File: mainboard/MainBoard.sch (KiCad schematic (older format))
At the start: 38 parts, among them J1 CONN_1x4, J2 CONN_2X3, J3 CONN_2X3, J5 SWDEBUG_CONNECTOR, J7 CONN_2X12, U1 VX07805-1000, U2 TPS2115A, U3 ld1117s33

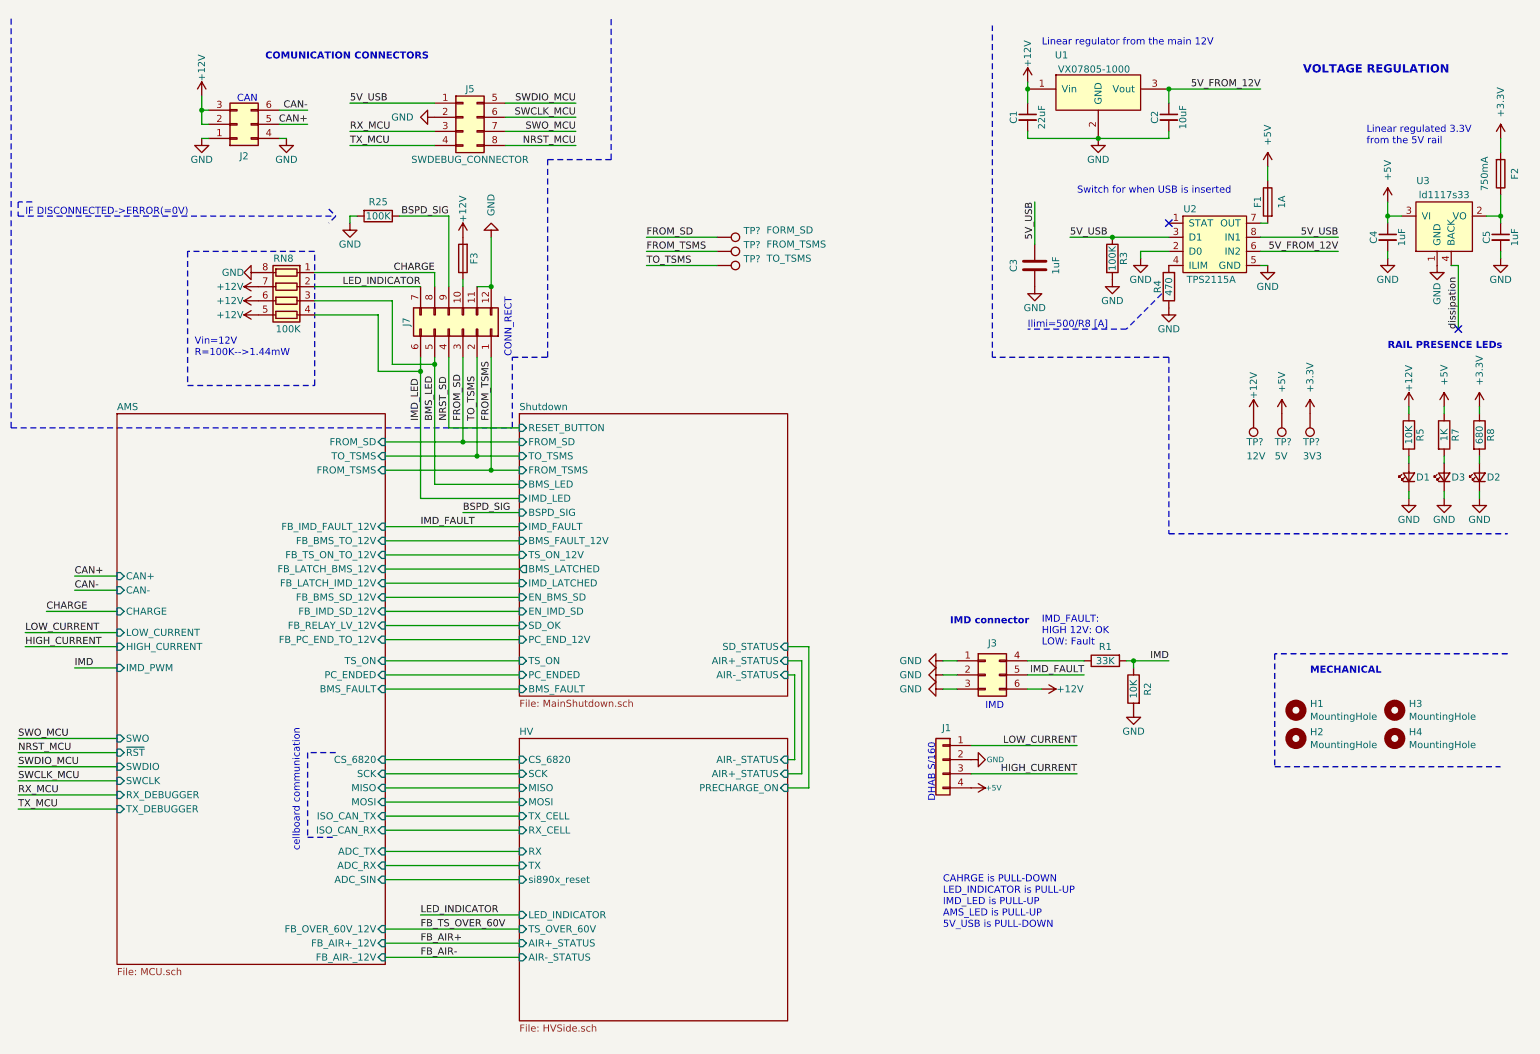
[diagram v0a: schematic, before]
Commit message: adding testpoints
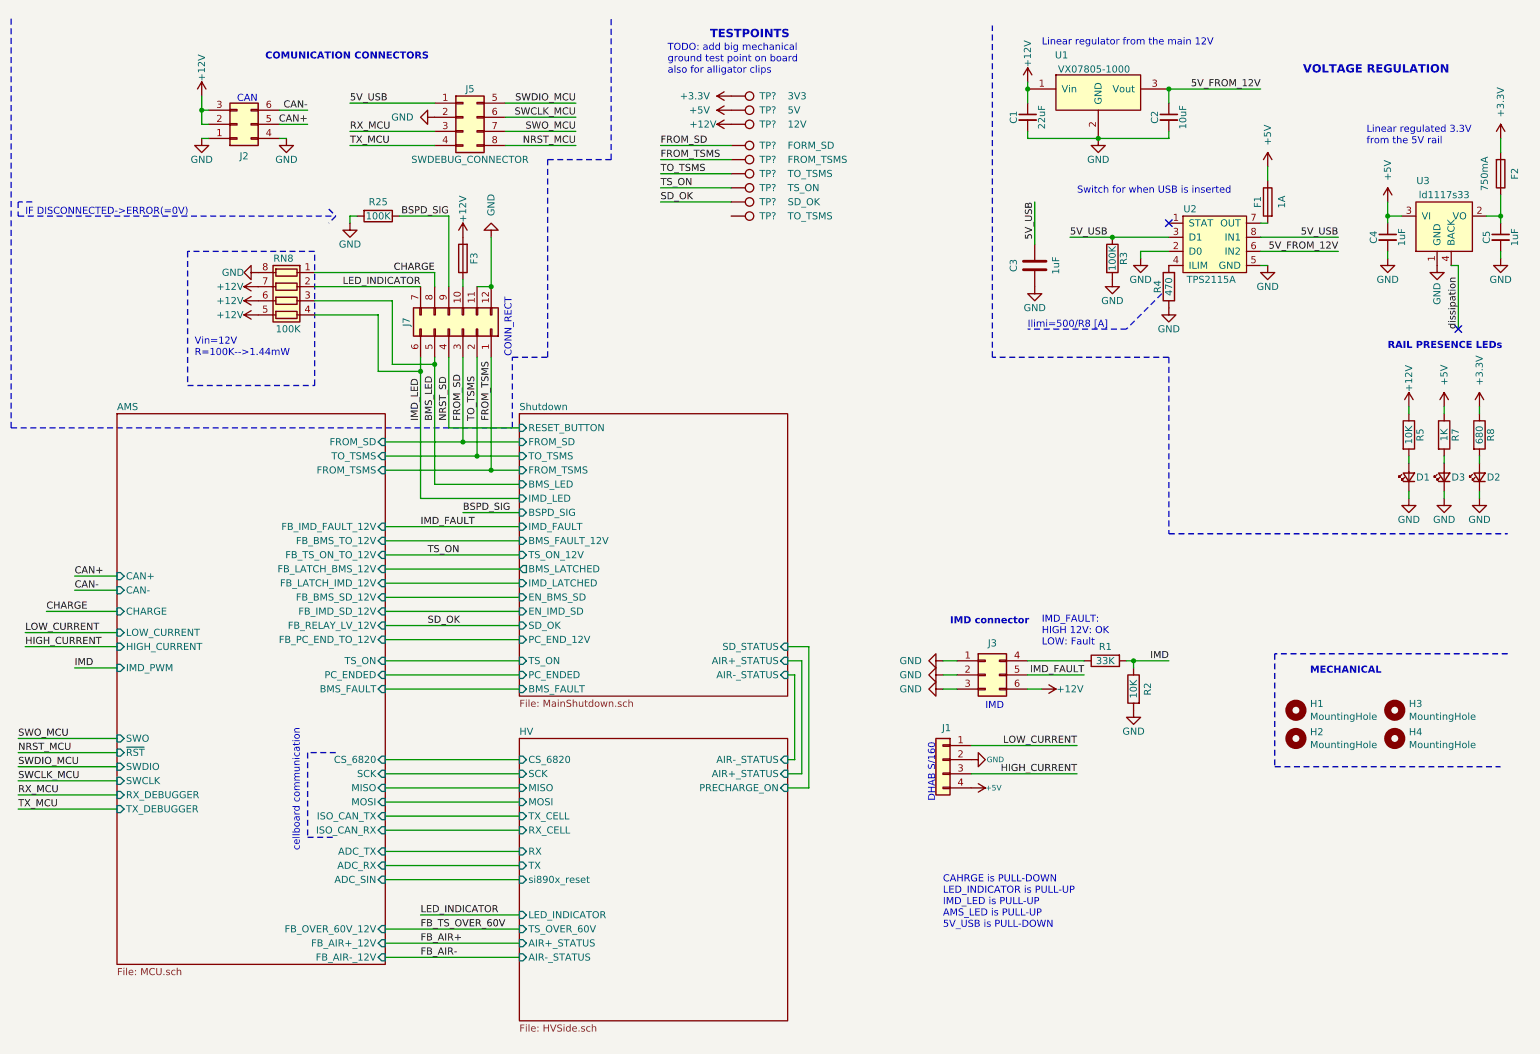
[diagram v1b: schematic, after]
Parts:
- removed TP?: 3V3, symbol Connector:TestPoint
- removed TP?: 5V, symbol Connector:TestPoint
- removed TP?: 12V, symbol Connector:TestPoint
- added TP?: TS_ON, symbol Connector:TestPoint
- added TP?: SD_OK, symbol Connector:TestPoint
- added TP?: TO_TSMS, symbol Connector:TestPoint
- added TP?: 3V3, symbol Connector:TestPoint
- added TP?: 5V, symbol Connector:TestPoint
- added TP?: 12V, symbol Connector:TestPoint
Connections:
- net +12V: now also TP?.1
- net +3V3: now also TP?.1
- net +5V: now also TP?.1
- new net SD_OK: TP?.1
- new net TS_ON: TP?.1
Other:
- note added: "TESTPOINTS"
- note added: "TODO: add big mechanical \nground test point on board\nalso for alligator clips"
- moved on the sheet: TP?
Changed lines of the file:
@@
 Text Notes 7800 5000 0    50   ~ 0
 IMD_FAULT:\nHIGH 12V: OK\nLOW: Fault
-Text Label 5000 2100 0    50   ~ 0
+Text Label 5100 1450 0    50   ~ 0
 FROM_SD
-Text Label 5000 2200 0    50   ~ 0
+Text Label 5100 1550 0    50   ~ 0
 FROM_TSMS
-Text Label 5000 2300 0    50   ~ 0
+Text Label 5100 1650 0    50   ~ 0
 TO_TSMS
 $Comp
 L Connector:TestPoint TP?
 U 1 1 605C7740
-P 5500 2100
-F 0 "TP?" V 5454 2288 50  0000 L CNN
-F 1 "FORM_SD" V 5450 2450 50  0000 L CNN
-F 2 "" H 5700 2100 50  0001 C CNN
-F 3 "~" H 5700 2100 50  0001 C CNN
-	1    5500 2100
+P 5600 1450
+F 0 "TP?" V 5600 1650 50  0000 L CNN
+F 1 "FORM_SD" V 5600 1850 50  0000 L CNN
+F 2 "" H 5800 1450 50  0001 C CNN
+F 3 "~" H 5800 1450 50  0001 C CNN
+	1    5600 1450
 	0    1    1    0
 $EndComp
@@
 L Connector:TestPoint TP?
 U 1 1 605C7DFE
-P 5500 2200
-F 0 "TP?" V 5454 2388 50  0000 L CNN
-F 1 "FROM_TSMS" V 5450 2550 50  0000 L CNN
-F 2 "" H 5700 2200 50  0001 C CNN
-F 3 "~" H 5700 2200 50  0001 C CNN
-	1    5500 2200
+P 5600 1550
+F 0 "TP?" V 5600 1750 50  0000 L CNN
+F 1 "FROM_TSMS" V 5600 1950 50  0000 L CNN
+F 2 "" H 5800 1550 50  0001 C CNN
+F 3 "~" H 5800 1550 50  0001 C CNN
+	1    5600 1550
 	0    1    1    0
 $EndComp
@@
 L Connector:TestPoint TP?
 U 1 1 605C7FA8
-P 5500 2300
-F 0 "TP?" V 5454 2488 50  0000 L CNN
-F 1 "TO_TSMS" V 5450 2650 50  0000 L CNN
-F 2 "" H 5700 2300 50  0001 C CNN
-F 3 "~" H 5700 2300 50  0001 C CNN
-	1    5500 2300
+P 5600 1650
+F 0 "TP?" V 5600 1850 50  0000 L CNN
+F 1 "TO_TSMS" V 5600 2050 50  0000 L CNN
+F 2 "" H 5800 1650 50  0001 C CNN
+F 3 "~" H 5800 1650 50  0001 C CNN
+	1    5600 1650
 	0    1    1    0
 $EndComp
 Wire Wire Line
-	5000 2100 5500 2100
+	5100 1450 5600 1450
 Wire Wire Line
-	5500 2200 5000 2200
+	5600 1550 5100 1550
 Wire Wire Line
-	5000 2300 5500 2300
-$Comp
-L Connector:TestPoint TP?
-U 1 1 6060C55B
-P 9700 3350
-F 0 "TP?" H 9750 3550 50  0000 R CNN
-F 1 "3V3" H 9750 3650 50  0000 R CNN
-F 2 "" H 9900 3350 50  0001 C CNN
-F 3 "~" H 9900 3350 50  0001 C CNN
-	1    9700 3350
-	-1   0    0    1
-$EndComp
-$Comp
-L Connector:TestPoint TP?
-U 1 1 6060CEE1
-P 9500 3350
-F 0 "TP?" H 9550 3550 50  0000 R CNN
-F 1 "5V" H 9550 3650 50  0000 R CNN
-F 2 "" H 9700 3350 50  0001 C CNN
-F 3 "~" H 9700 3350 50  0001 C CNN
-	1    9500 3350
-	-1   0    0    1
-$EndComp
-$Comp
-L Connector:TestPoint TP?
-U 1 1 6060D124
-P 9300 3350
-F 0 "TP?" H 9350 3550 50  0000 R CNN
-F 1 "12V" H 9350 3650 50  0000 R CNN
-F 2 "" H 9500 3350 50  0001 C CNN
-F 3 "~" H 9500 3350 50  0001 C CNN
-	1    9300 3350
-	-1   0    0    1
-$EndComp
+	5100 1650 5600 1650
 $Comp
 L power:+12V #PWR?
 U 1 1 6061F869
-P 9300 3350
+P 5600 1300
 AR Path="/6061F869" Ref="#PWR?"  Part="1"
 AR Path="/5DE633EC/6061F869" Ref="#PWR?"  Part="1"
-F 0 "#PWR?" H 9300 3200 50  0001 C CNN
-F 1 "+12V" V 9300 3550 50  0000 C CNN
-F 2 "" H 9300 3350 50  0001 C CNN
-F 3 "" H 9300 3350 50  0001 C CNN
-	1    9300 3350
-	1    0    0    -1
+F 0 "#PWR?" H 5600 1150 50  0001 C CNN
+F 1 "+12V" V 5600 1500 50  0000 C CNN
+F 2 "" H 5600 1300 50  0001 C CNN
+F 3 "" H 5600 1300 50  0001 C CNN
+	1    5600 1300
+	0    -1   -1   0
 $EndComp
 $Comp
 L power:+5V #PWR?
 U 1 1 6061F86F
-P 9500 3350
+P 5600 1200
 AR Path="/6061F86F" Ref="#PWR?"  Part="1"
 AR Path="/5DE633EC/6061F86F" Ref="#PWR?"  Part="1"
-F 0 "#PWR?" H 9500 3200 50  0001 C CNN
-F 1 "+5V" V 9500 3500 50  0000 L CNN
-F 2 "" H 9500 3350 50  0001 C CNN
-F 3 "" H 9500 3350 50  0001 C CNN
-	1    9500 3350
-	1    0    0    -1
+F 0 "#PWR?" H 5600 1050 50  0001 C CNN
+F 1 "+5V" V 5600 1350 50  0000 L CNN
+F 2 "" H 5600 1200 50  0001 C CNN
+F 3 "" H 5600 1200 50  0001 C CNN
+	1    5600 1200
+	0    -1   -1   0
 $EndComp
 $Comp
 L power:+3.3V #PWR?
 U 1 1 6061F875
-P 9700 3350
+P 5600 1100
 AR Path="/6061F875" Ref="#PWR?"  Part="1"
 AR Path="/5DE633EC/6061F875" Ref="#PWR?"  Part="1"
-F 0 "#PWR?" H 9700 3200 50  0001 C CNN
-F 1 "+3.3V" V 9700 3500 50  0000 L CNN
-F 2 "" H 9700 3350 50  0001 C CNN
-F 3 "" H 9700 3350 50  0001 C CNN
-	1    9700 3350
-	1    0    0    -1
+F 0 "#PWR?" H 5600 950 50  0001 C CNN
+F 1 "+3.3V" V 5600 1250 50  0000 L CNN
+F 2 "" H 5600 1100 50  0001 C CNN
+F 3 "" H 5600 1100 50  0001 C CNN
+	1    5600 1100
+	0    -1   -1   0
 $EndComp
 Wire Notes Line
@@
 Wire Notes Line
 	8700 2950 8700 4200
+$Comp
+L Connector:TestPoint TP?
+U 1 1 604E0BCB
+P 5600 1750
+F 0 "TP?" V 5600 1950 50  0000 L CNN
+F 1 "TS_ON" V 5600 2150 50  0000 L CNN
+F 2 "" H 5800 1750 50  0001 C CNN
+F 3 "~" H 5800 1750 50  0001 C CNN
+	1    5600 1750
+	0    1    1    0
+$EndComp
+$Comp
+L Connector:TestPoint TP?
+U 1 1 604E0D6B
+P 5600 1850
+F 0 "TP?" V 5600 2050 50  0000 L CNN
+F 1 "SD_OK" V 5600 2250 50  0000 L CNN
+F 2 "" H 5800 1850 50  0001 C CNN
+F 3 "~" H 5800 1850 50  0001 C CNN
+	1    5600 1850
+	0    1    1    0
+$EndComp
+$Comp
+L Connector:TestPoint TP?
+U 1 1 604E0F65
+P 5600 1950
+F 0 "TP?" V 5600 2150 50  0000 L CNN
+F 1 "TO_TSMS" V 5600 2350 50  0000 L CNN
+F 2 "" H 5800 1950 50  0001 C CNN
+F 3 "~" H 5800 1950 50  0001 C CNN
+	1    5600 1950
+	0    1    1    0
+$EndComp
+Text Label 3450 4850 0    50   ~ 0
+SD_OK
+Text Label 3450 4350 0    50   ~ 0
+TS_ON
+Text Label 5100 1850 0    50   ~ 0
+SD_OK
+Text Label 5100 1750 0    50   ~ 0
+TS_ON
+Wire Wire Line
+	5100 1750 5600 1750
+Wire Wire Line
+	5600 1850 5100 1850
+Text Notes 5450 700  0    59   ~ 12
+TESTPOINTS
+$Comp
+L Connector:TestPoint TP?
+U 1 1 6052AFD5
+P 5600 1100
+F 0 "TP?" V 5600 1300 50  0000 L CNN
+F 1 "3V3" V 5600 1500 50  0000 L CNN
+F 2 "" H 5800 1100 50  0001 C CNN
+F 3 "~" H 5800 1100 50  0001 C CNN
+	1    5600 1100
+	0    1    1    0
+$EndComp
+$Comp
+L Connector:TestPoint TP?
+U 1 1 6052B327
+P 5600 1200
+F 0 "TP?" V 5600 1400 50  0000 L CNN
+F 1 "5V" V 5600 1600 50  0000 L CNN
+F 2 "" H 5800 1200 50  0001 C CNN
+F 3 "~" H 5800 1200 50  0001 C CNN
+	1    5600 1200
+	0    1    1    0
+$EndComp
+$Comp
+L Connector:TestPoint TP?
+U 1 1 6052B600
+P 5600 1300
+F 0 "TP?" V 5600 1500 50  0000 L CNN
+F 1 "12V" V 5600 1700 50  0000 L CNN
+F 2 "" H 5800 1300 50  0001 C CNN
+F 3 "~" H 5800 1300 50  0001 C CNN
+	1    5600 1300
+	0    1    1    0
+$EndComp
+Text Notes 5150 950  0    50   ~ 0
+TODO: add big mechanical \nground test point on board\nalso for alligator clips
 $EndSCHEMATC

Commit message: new standard connector
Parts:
- J5: footprint MainBoard:Molex_Nano-Fit_105310-xx08_2x04_P2.50mm_Vertical -> MainBoard:Molex_Nano-Fit_105310-xx08_2x05_P2.50mm_Vertical; symbol Connector_Generic:Conn_02x04_Top_Bottom -> Connector_Generic:Conn_02x05_Top_Bottom
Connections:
- net +3V3: now also J5.4 (Pin_4)
- net 5V_USB: now also J5.9 (Pin_9); no longer J5.1 (Pin_1)
- net GND: now also J5.1 (Pin_1), J5.6 (Pin_6); no longer J5.2 (Pin_2)
- net NRST_MCU: now also J5.7 (Pin_7); no longer J5.8 (Pin_8)
- net RX_MCU: now also J5.10 (Pin_10); no longer J5.3 (Pin_3)
- net SWCLK_MCU: now also J5.2 (Pin_2); no longer J5.6 (Pin_6)
- net SWDIO_MCU: now also J5.3 (Pin_3); no longer J5.5 (Pin_5)
- net SWO_MCU: now also J5.8 (Pin_8); no longer J5.7 (Pin_7)
- net TX_MCU: now also J5.5 (Pin_5); no longer J5.4 (Pin_4)
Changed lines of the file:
@@
 Wire Wire Line
 	2650 2550 3200 2550
-Text Label 2900 1150 0    50   ~ 0
+Text Label 4500 1350 2    50   ~ 0
 5V_USB
 $Comp
 L power:GND #PWR0116
 U 1 1 5E56B74E
-P 3500 1250
+P 3500 1050
 AR Path="/5E56B74E" Ref="#PWR0116"  Part="1"
 AR Path="/5DE633EC/5E56B74E" Ref="#PWR?"  Part="1"
-F 0 "#PWR0116" H 3500 1000 50  0001 C CNN
-F 1 "GND" V 3500 1100 50  0000 R CNN
-F 2 "" H 3500 1250 50  0001 C CNN
-F 3 "" H 3500 1250 50  0001 C CNN
-	1    3500 1250
+F 0 "#PWR0116" H 3500 800 50  0001 C CNN
+F 1 "GND" V 3500 900 50  0000 R CNN
+F 2 "" H 3500 1050 50  0001 C CNN
+F 3 "" H 3500 1050 50  0001 C CNN
+	1    3500 1050
 	0    1    -1   0
 $EndComp
 Wire Wire Line
+	4500 1150 4000 1150
+Wire Wire Line
+	3000 1250 3500 1250
+Wire Wire Line
+	3000 1150 3500 1150
+Wire Wire Line
 	4500 1450 4000 1450
-Wire Wire Line
-	4500 1150 4000 1150
-Wire Wire Line
-	4500 1250 4000 1250
-Wire Wire Line
-	2900 1350 3500 1350
+Text Label 4500 1150 2    50   ~ 0
+NRST_MCU
+Text Label 3000 1250 0    50   ~ 0
+SWDIO_MCU
+Text Label 3000 1150 0    50   ~ 0
+SWCLK_MCU
 Text Label 4500 1450 2    50   ~ 0
-NRST_MCU
-Text Label 4500 1150 2    50   ~ 0
-SWDIO_MCU
-Text Label 4500 1250 2    50   ~ 0
-SWCLK_MCU
-Text Label 2900 1350 0    50   ~ 0
 RX_MCU
 Wire Wire Line
@@
 Wire Wire Line
 	550  5650 1250 5650
-Text Label 4500 1350 2    50   ~ 0
+Text Label 4500 1250 2    50   ~ 0
 SWO_MCU
 Wire Wire Line
-	4500 1350 4000 1350
+	4500 1250 4000 1250
 $Sheet
 S 4100 5650 1900 2000
@@
 $EndSheet
 $Comp
-L Connector_Generic:Conn_02x04_Top_Bottom J5
+L Connector_Generic:Conn_02x05_Top_Bottom J5
 U 1 1 5E5F21A9
 P 3700 1250
 F 0 "J5" H 3750 1450 50  0000 C CNN
 F 1 "SWDEBUG_CONNECTOR" H 3750 950 50  0000 C CNN
-F 2 "MainBoard:Molex_Nano-Fit_105310-xx08_2x04_P2.50mm_Vertical" H 3700 1250 50  0001 C CNN
+F 2 "MainBoard:Molex_Nano-Fit_105310-xx08_2x05_P2.50mm_Vertical" H 3700 1250 50  0001 C CNN
 F 3 "~" H 3700 1250 50  0001 C CNN
 	1    3700 1250
 	1    0    0    -1
 $EndComp
-Text Label 2900 1450 0    50   ~ 0
+Text Label 3000 1450 0    50   ~ 0
 TX_MCU
 Wire Wire Line
-	2900 1450 3500 1450
+	3000 1450 3500 1450
 $Comp
 L Connector_Generic:Conn_02x03_Top_Bottom J2
@@
 	11050 1400 11050 1500
 Wire Wire Line
-	2900 1150 3500 1150
+	4500 1350 4000 1350
 $Comp
 L power:GND #PWR0239
@@
 Text Notes 5150 950  0    50   ~ 0
 TODO: add big mechanical \nground test point on board\nalso for alligator clips
+$Comp
+L power:GND #PWR?
+U 1 1 6081955F
+P 4000 1050
+AR Path="/6081955F" Ref="#PWR?"  Part="1"
+AR Path="/5DE633EC/6081955F" Ref="#PWR?"  Part="1"
+F 0 "#PWR?" H 4000 800 50  0001 C CNN
+F 1 "GND" V 4000 900 50  0000 R CNN
+F 2 "" H 4000 1050 50  0001 C CNN
+F 3 "" H 4000 1050 50  0001 C CNN
+	1    4000 1050
+	0    -1   1    0
+$EndComp
+$Comp
+L power:+3.3V #PWR?
+U 1 1 608528CD
+P 3500 1350
+AR Path="/608528CD" Ref="#PWR?"  Part="1"
+AR Path="/5DE633EC/608528CD" Ref="#PWR?"  Part="1"
+F 0 "#PWR?" H 3500 1200 50  0001 C CNN
+F 1 "+3.3V" V 3500 1500 50  0000 L CNN
+F 2 "" H 3500 1350 50  0001 C CNN
+F 3 "" H 3500 1350 50  0001 C CNN
+	1    3500 1350
+	0    -1   -1   0
+$EndComp
 $EndSCHEMATC

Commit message: v1.1 as printed
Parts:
- removed C1: 22uF, Capacitor_SMD:C_1206_3216Metric, symbol Device:C_Small
- removed C2: 10uF, Capacitor_SMD:C_0805_2012Metric, symbol Device:C_Small
- removed C3: 1uF, Capacitor_SMD:C_0805_2012Metric, symbol Device:C
- removed C4, C5: 1uF, Capacitor_SMD:C_0805_2012Metric, symbol Device:C_Small
- removed R3: 100K, Resistor_SMD:R_0603_1608Metric, symbol Device:R
- removed R4: 470, Resistor_SMD:R_0603_1608Metric, symbol Device:R
- removed TP?: TS_ON, symbol Connector:TestPoint
- removed TP?: SD_OK, symbol Connector:TestPoint
- removed TP?: TO_TSMS, symbol Connector:TestPoint
- removed U1: VX07805-1000, MainBoard:DC_DC_VXO7805_1000, symbol MainBoard:NCV5501
- removed U2: TPS2115A, Package_SO:TSSOP-8_4.4x3mm_P0.65mm, symbol MainBoard:TPS2115A
- removed U3: ld1117s33, Package_TO_SOT_SMD:SOT-223, symbol MainBoard:LD1117S33
- added H5: MountingHole, MountingHole:MountingHole_3mm, symbol Mechanical:MountingHole
- added JP2: 3V3_PROG, Jumper:SolderJumper-2_P1.3mm_Open_RoundedPad1.0x1.5mm, symbol Jumper:SolderJumper_2_Open
- added R35: 120, Resistor_SMD:R_0805_2012Metric, symbol Device:R
- added TP29, TP30: GND, MainBoard:TestPoint_GNDedge, symbol Connector:TestPoint
- added TP35: IMD_PWM, TestPoint:TestPoint_Pad_D1.0mm, symbol Connector:TestPoint
- added TP7: BSPD_SIG, TestPoint:TestPoint_Pad_D1.0mm, symbol Connector:TestPoint
- added TP8: IMD_FAULT, TestPoint:TestPoint_Pad_D1.0mm, symbol Connector:TestPoint
- added U1: Tex_DCDC, MainBoard:Tex_DCDC_vertical, symbol MainBoard:Tex_DCDC
- J5: footprint MainBoard:Molex_Nano-Fit_105310-xx08_2x05_P2.50mm_Vertical -> Connector_Molex:Molex_Nano-Fit_105310-xx10_2x05_P2.50mm_Vertical
- TP1, TP2, TP3, TP5, TP6: renamed from TP?; footprint (none) -> TestPoint:TestPoint_Pad_D1.0mm
- TP4: renamed from TP?; value FORM_SD -> FROM_SD; footprint (none) -> TestPoint:TestPoint_Pad_D1.0mm
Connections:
- net +12V: now also U1.4 (12V); no longer RN8.5 (R4.2), RN8.6 (R3.2), RN8.7 (R2.2)
- net +3V3: no longer J5.4 (Pin_4)
- net BSPD_SIG: now also R25.2, TP7.1; no longer R25.1
- net CAN+: now also R35.1
- net CAN-: now also R35.2
- net GND: now also R25.1, RN8.5 (R4.2), RN8.6 (R3.2), RN8.7 (R2.2), TP29.1, TP30.1, U1.2 (GND), U1.6 (GND); no longer R25.2
- net IMD_FAULT: now also TP8.1
- net 3V3_prefuse: now reaches F2.1
- net 3V3_prefuse: now also JP2.1 (A), U1.1 (3V3)
- net at F1.2: now also U1.3 (5V)
- net 5V_USB renamed 5V_PROG
- net 5V_PROG: now also U1.5 (USB)
- net IMD renamed IMD_PWM
- net IMD_PWM: now also TP35.1
- net LED_INDICATOR renamed TSAL
- new net: J5.4 (Pin_4), JP2.2 (B)
- no-connect marks 2 -> 0
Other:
- note added: "CHARGE is PULL-DOWN\nTSAL is PULL-DOWN\nIMD_LED is PULL-DOWN\nAMS_LED is PULL-DOWN\n5V_PROG is PULL-DOWN"
- note added: "DNP"
- note added: "TSAL = HIGH safe, LOW unsafe\n(IMD_LED = HIGH safe, LOW unsafe\nBMS_LED = HIGH safe, LOW unsafe)"
- note added: "adc comm"
- note added: "cells com"
- note added: "feedbacks"
- note removed: "CAHRGE is PULL-DOWN\nLED_INDICATOR is PULL-UP\nIMD_LED is PULL-UP\nAMS_LED is PULL-UP\n5V_USB is PULL-DOWN"
- note removed: "CONN_RECT"
- note removed: "Ilimi=500/R8 [A]"
- note removed: "Linear regulated 3.3V \nfrom the 5V rail"
- note removed: "Linear regulator from the main 12V"
- note removed: "Switch for when USB is inserted"
- note removed: "TESTPOINTS"
- note removed: "TODO: add big mechanical \nground test point on board\nalso for alligator clips"
- note removed: "Vin=12V\nR=100K-->1.44mW"
- note removed: "cellboard communication"
- moved on the sheet: D1, D2, D3, F1, F2, F3, H1, H2, H3, H4, J1, J2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
